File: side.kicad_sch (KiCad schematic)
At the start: 53 parts, among them SW10 SW_Push, SW11 SW_Push, SW12 SW_Push, SW13 SW_Push, SW14 SW_Push, SW15 SW_Push, SW16 SW_Push, SW17 SW_Push, SW18 SW_Push, SW19 SW_Push, SW20 SW_Push, SW21 SW_Push, SW22 SW_Push, SW23 SW_Push, SW3 SW_Push, SW4 SW_Push, SW5 SW_Push, SW6 SW_Push, SW7 SW_Push, SW8 SW_Push, SW9 SW_Push, U1 XIAO-nRF52840-SMD

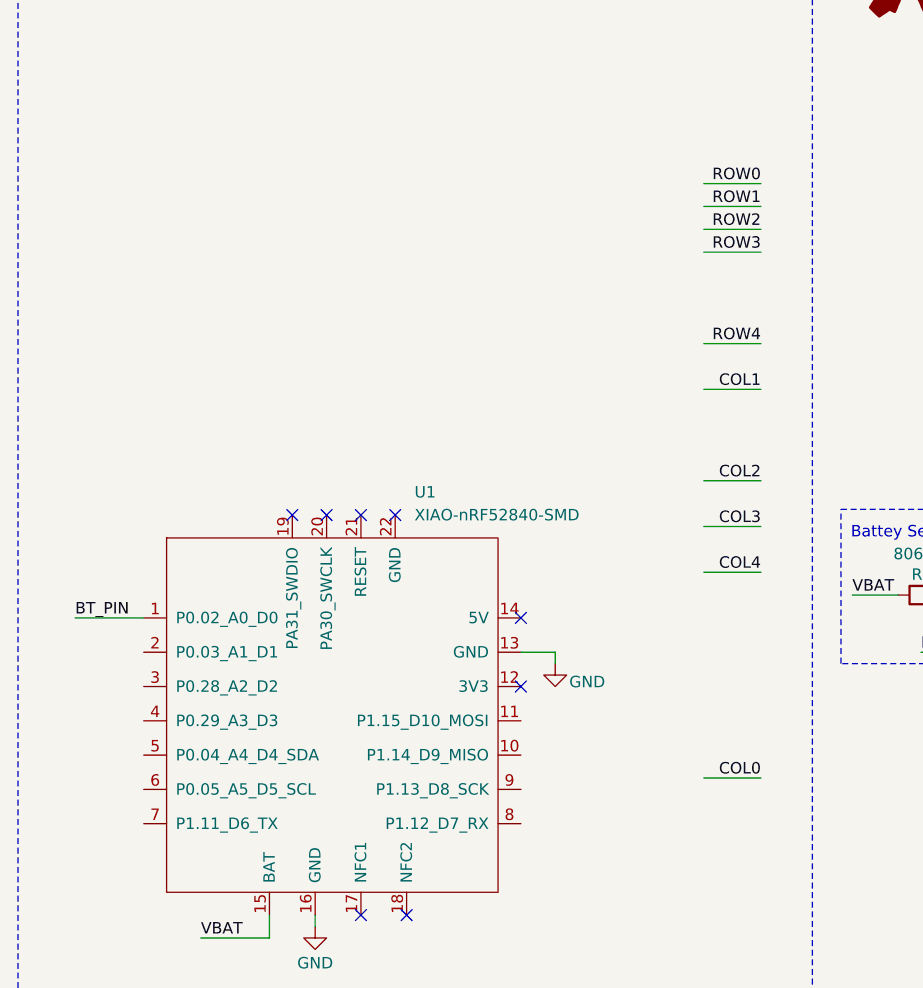
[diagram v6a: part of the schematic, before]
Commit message: changed xioa footprint, edited edge cuts, layed out
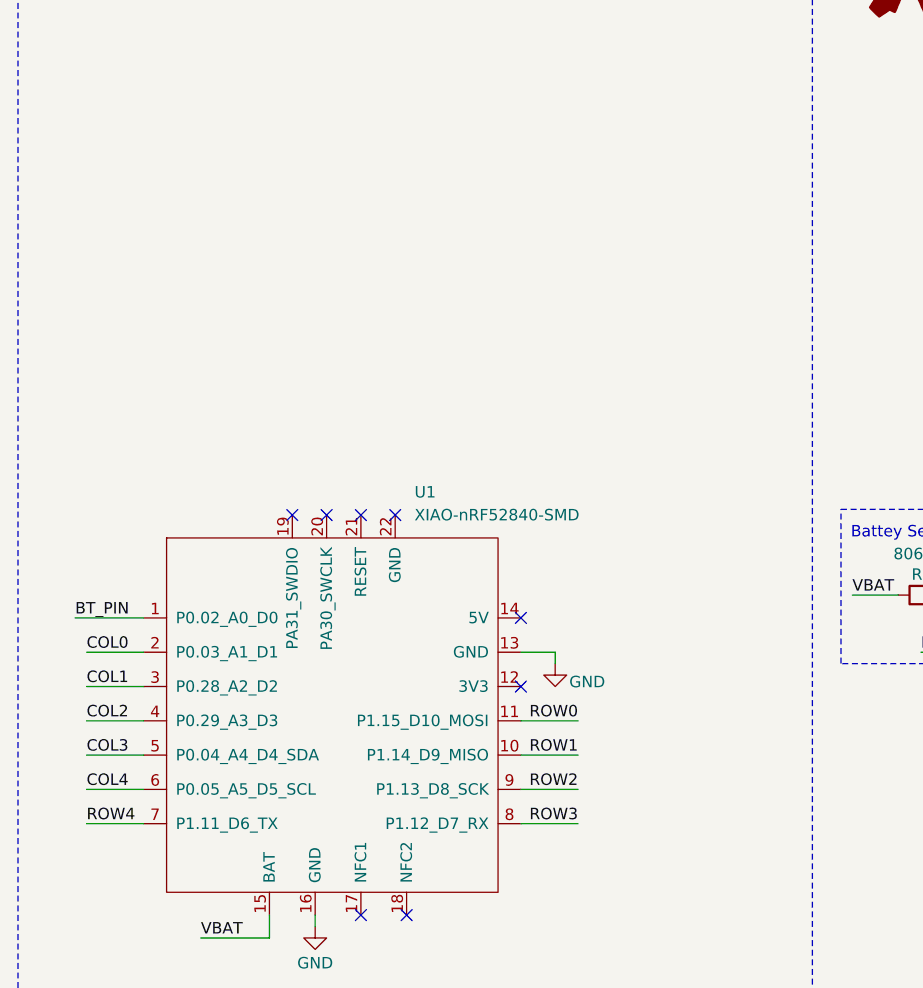
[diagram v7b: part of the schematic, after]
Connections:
- net COL0: now also U1.2 (P0.03_A1_D1)
- net COL1: now also U1.3 (P0.28_A2_D2)
- net COL2: now also U1.4 (P0.29_A3_D3)
- net COL3: now also U1.5 (P0.04_A4_D4_SDA)
- net COL4: now also U1.6 (P0.05_A5_D5_SCL)
- net ROW0: now also U1.11 (P1.15_D10_MOSI)
- net ROW1: now also U1.10 (P1.14_D9_MISO)
- net ROW2: now also U1.9 (P1.13_D8_SCK)
- net ROW3: now also U1.8 (P1.12_D7_RX)
- net ROW4: now also U1.7 (P1.11_D6_TX)
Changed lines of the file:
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@@
 	(wire
 		(pts
-			(xy 96.52 48.26) (xy 90.17 48.26)
+			(xy 76.2 110.49) (xy 69.85 110.49)
 		)
 		(stroke
@@
 	(wire
 		(pts
-			(xy 96.52 50.8) (xy 90.17 50.8)
+			(xy 76.2 114.3) (xy 69.85 114.3)
 		)
 		(stroke
@@
 	(wire
 		(pts
-			(xy 96.52 66.04) (xy 90.17 66.04)
+			(xy 21.59 99.06) (xy 27.94 99.06)
 		)
 		(stroke
@@
 	(wire
 		(pts
-			(xy 96.52 43.18) (xy 90.17 43.18)
+			(xy 76.2 102.87) (xy 69.85 102.87)
 		)
 		(stroke
@@
 	(wire
 		(pts
-			(xy 96.52 76.2) (xy 90.17 76.2)
+			(xy 21.59 102.87) (xy 27.94 102.87)
 		)
 		(stroke
@@
 	(wire
 		(pts
-			(xy 96.52 60.96) (xy 90.17 60.96)
+			(xy 21.59 114.3) (xy 27.94 114.3)
 		)
 		(stroke
@@
 	(wire
 		(pts
-			(xy 96.52 109.22) (xy 90.17 109.22)
+			(xy 21.59 95.25) (xy 27.94 95.25)
 		)
 		(stroke
@@
 	(wire
 		(pts
-			(xy 96.52 45.72) (xy 90.17 45.72)
+			(xy 76.2 106.68) (xy 69.85 106.68)
 		)
 		(stroke
@@
 	(wire
 		(pts
-			(xy 96.52 81.28) (xy 90.17 81.28)
+			(xy 21.59 106.68) (xy 27.94 106.68)
 		)
 		(stroke
@@
 	(wire
 		(pts
-			(xy 96.52 86.36) (xy 90.17 86.36)
+			(xy 21.59 110.49) (xy 27.94 110.49)
 		)
 		(stroke
@@
 	)
 	(label "COL1"
-		(at 96.52 66.04 180)
-		(effects
-			(font
-				(size 1.27 1.27)
-			)
-			(justify right bottom)
+		(at 21.59 99.06 0)
+		(effects
+			(font
+				(size 1.27 1.27)
+			)
+			(justify left bottom)
 		)
 	)
@@
 	)
 	(label "ROW0"
-		(at 96.52 43.18 180)
+		(at 76.2 102.87 180)
 		(effects
 			(font
@@
 	)
 	(label "ROW3"
-		(at 96.52 50.8 180)
+		(at 76.2 114.3 180)
 		(effects
 			(font
@@
 	)
 	(label "COL3"
-		(at 96.52 81.28 180)
-		(effects
-			(font
-				(size 1.27 1.27)
-			)
-			(justify right bottom)
+		(at 21.59 106.68 0)
+		(effects
+			(font
+				(size 1.27 1.27)
+			)
+			(justify left bottom)
 		)
 	)
@@
 	)
 	(label "ROW4"
-		(at 96.52 60.96 180)
-		(effects
-			(font
-				(size 1.27 1.27)
-			)
-			(justify right bottom)
+		(at 21.59 114.3 0)
+		(effects
+			(font
+				(size 1.27 1.27)
+			)
+			(justify left bottom)
 		)
 	)
@@
 	)
 	(label "COL4"
-		(at 96.52 86.36 180)
+		(at 21.59 110.49 0)
+		(effects
+			(font
+				(size 1.27 1.27)
+			)
+			(justify left bottom)
+		)
+	)
+	(label "COL2"
+		(at 21.59 102.87 0)
+		(effects
+			(font
+				(size 1.27 1.27)
+			)
+			(justify left bottom)
+		)
+	)
+	(label "ROW2"
+		(at 76.2 110.49 180)
 		(effects
 			(font
@@
 		)
 	)
-	(label "COL2"
-		(at 96.52 76.2 180)
-		(effects
-			(font
-				(size 1.27 1.27)
-			)
-			(justify right bottom)
-		)
-	)
-	(label "ROW2"
-		(at 96.52 48.26 180)
-		(effects
-			(font
-				(size 1.27 1.27)
-			)
-			(justify right bottom)
-		)
-	)
 	(label "COL0"
-		(at 96.52 109.22 180)
-		(effects
-			(font
-				(size 1.27 1.27)
-			)
-			(justify right bottom)
+		(at 21.59 95.25 0)
+		(effects
+			(font
+				(size 1.27 1.27)
+			)
+			(justify left bottom)
 		)
 	)
@@
 	)
 	(label "ROW1"
-		(at 96.52 45.72 180)
-		(effects
-			(font
+		(at 76.2 106.68 180)
+		(effects
+			(font

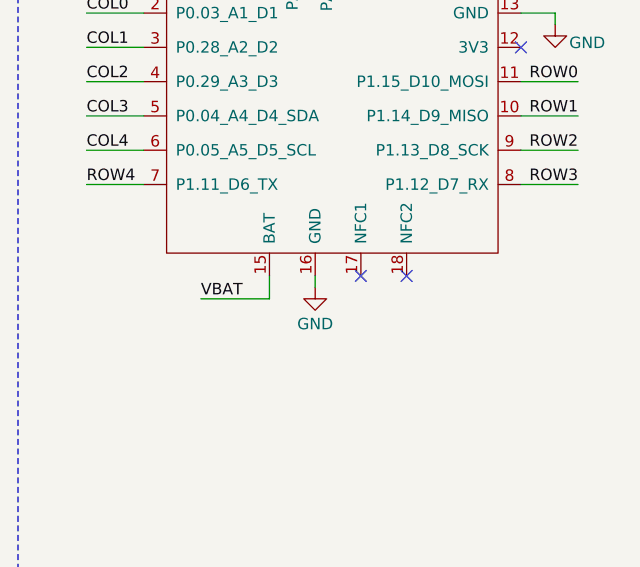
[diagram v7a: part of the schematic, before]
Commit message: routed left half
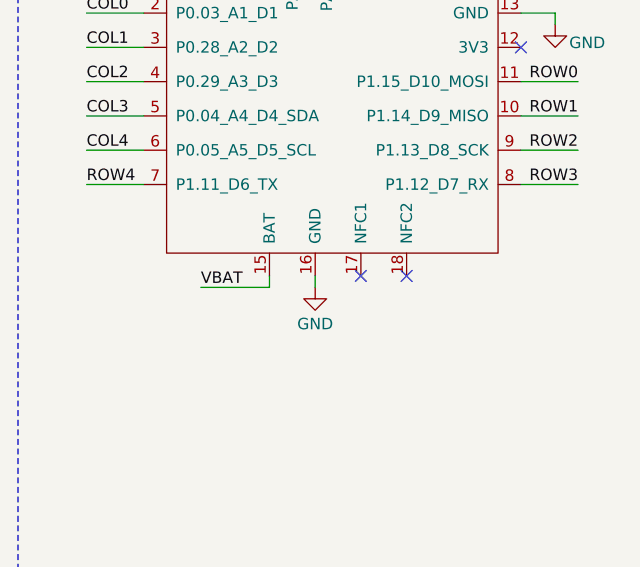
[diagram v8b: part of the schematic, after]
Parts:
- U1: footprint Seeed Studio XIAO Series Library:XIAO-nRF52840-SMD -> mito-simplified:XIAO-nRF52840-SMD
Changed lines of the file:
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@@
 	(wire
 		(pts
-			(xy 41.91 127) (xy 41.91 124.46)
+			(xy 41.91 125.73) (xy 41.91 124.46)
 		)
 		(stroke
@@
 	(wire
 		(pts
-			(xy 34.29 127) (xy 41.91 127)
+			(xy 34.29 125.73) (xy 41.91 125.73)
 		)
 		(stroke
@@
 	)
 	(label "VBAT"
-		(at 34.29 127 0)
+		(at 34.29 125.73 0)
 		(effects
 			(font
@@
 			)
 		)
-		(property "Footprint" "Seeed Studio XIAO Series Library:XIAO-nRF52840-SMD"
+		(property "Footprint" "mito-simplified:XIAO-nRF52840-SMD"
 			(at 40.64 97.79 0)
 			(effects
